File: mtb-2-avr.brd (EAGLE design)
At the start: 27 x 22 mm, 14 parts, among them IC1 MEGA8-AI, Q1 14.745 MHz

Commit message: Add LCSC parts numbers.
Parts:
- IC1: value MEGA8-AI -> MEGA328P-AU
- R3: value 1k -> 10k
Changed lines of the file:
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@@
 <layer number="20" name="Dimension" color="24" fill="1" visible="yes" active="yes"/>
 <layer number="21" name="tPlace" color="7" fill="1" visible="yes" active="yes"/>
-<layer number="22" name="bPlace" color="7" fill="1" visible="no" active="yes"/>
+<layer number="22" name="bPlace" color="7" fill="1" visible="yes" active="yes"/>
 <layer number="23" name="tOrigins" color="15" fill="1" visible="yes" active="yes"/>
-<layer number="24" name="bOrigins" color="15" fill="1" visible="no" active="yes"/>
+<layer number="24" name="bOrigins" color="15" fill="1" visible="yes" active="yes"/>
 <layer number="25" name="tNames" color="7" fill="1" visible="no" active="yes"/>
 <layer number="26" name="bNames" color="7" fill="1" visible="no" active="yes"/>
@@
 <layer number="37" name="tTest" color="7" fill="1" visible="no" active="yes"/>
 <layer number="38" name="bTest" color="7" fill="1" visible="no" active="yes"/>
-<layer number="39" name="tKeepout" color="4" fill="11" visible="yes" active="yes"/>
-<layer number="40" name="bKeepout" color="1" fill="11" visible="yes" active="yes"/>
+<layer number="39" name="tKeepout" color="4" fill="11" visible="no" active="yes"/>
+<layer number="40" name="bKeepout" color="1" fill="11" visible="no" active="yes"/>
 <layer number="41" name="tRestrict" color="4" fill="10" visible="no" active="yes"/>
 <layer number="42" name="bRestrict" color="1" fill="10" visible="no" active="yes"/>
@@
 <layer number="44" name="Drills" color="7" fill="1" visible="no" active="yes"/>
 <layer number="45" name="Holes" color="7" fill="1" visible="no" active="yes"/>
-<layer number="46" name="Milling" color="3" fill="1" visible="no" active="yes"/>
+<layer number="46" name="Milling" color="3" fill="1" visible="yes" active="yes"/>
 <layer number="47" name="Measures" color="7" fill="1" visible="no" active="yes"/>
 <layer number="48" name="Document" color="7" fill="1" visible="no" active="yes"/>
-<layer number="49" name="Reference" color="7" fill="1" visible="no" active="yes"/>
+<layer number="49" name="Reference" color="7" fill="1" visible="yes" active="yes"/>
 <layer number="50" name="dxf" color="7" fill="1" visible="no" active="no"/>
 <layer number="51" name="tDocu" color="7" fill="1" visible="yes" active="yes"/>
-<layer number="52" name="bDocu" color="7" fill="1" visible="no" active="yes"/>
+<layer number="52" name="bDocu" color="7" fill="1" visible="yes" active="yes"/>
 <layer number="53" name="tGND_GNDA" color="7" fill="9" visible="no" active="no"/>
 <layer number="54" name="bGND_GNDA" color="1" fill="9" visible="no" active="no"/>
@@
 <text x="5.715" y="3.81" size="1.016" layer="22" rot="MR0" align="bottom-center">MTB-UNI
 v2 upgrade</text>
-<text x="24.765" y="16.51" size="1.016" layer="26" rot="MR90" align="bottom-center">v1.0 JH 2021</text>
+<text x="24.765" y="16.51" size="1.016" layer="22" rot="MR90" align="bottom-center">v1.0 JH 2021</text>
 <text x="4.1275" y="16.1925" size="1.27" layer="21" rot="SR180">⏚</text>
 </plain>
@@
 </autorouter>
 <elements>
-<element name="IC1" library="atmel" library_urn="urn:adsk.eagle:library:105" package="TQFP32-08" package3d_urn="urn:adsk.eagle:package:4313/2" value="MEGA8-AI" x="17.145" y="15.875" smashed="yes" rot="R180">
+<element name="IC1" library="atmel" library_urn="urn:adsk.eagle:library:105" package="TQFP32-08" package3d_urn="urn:adsk.eagle:package:4313/2" value="MEGA328P-AU" x="17.145" y="15.875" smashed="yes" rot="R180">
+<attribute name="LCSC_PART" value="C14877" x="17.145" y="15.875" size="1.778" layer="27" rot="R180" display="off"/>
 <attribute name="MF" value="" x="-0.635" y="20.955" size="1.778" layer="27" rot="R180" display="off"/>
 <attribute name="MPN" value="ATMEGA8-16AU" x="-0.635" y="20.955" size="1.778" layer="27" rot="R180" display="off"/>
@@
 <element name="TORIG" library="mtb-2" package="DIL20" value="" x="13.335" y="5.08" smashed="yes"/>
 <element name="C1" library="rcl" package="C0603" value="100n" x="24.765" y="16.1925" smashed="yes" rot="R270">
+<attribute name="LCSC_PART" value="C14663" x="24.765" y="16.1925" size="1.778" layer="27" rot="R270" display="off"/>
 <attribute name="NAME" x="25.7175" y="16.8275" size="0.8128" layer="25" rot="R270"/>
 <attribute name="VALUE" x="22.225" y="17.4625" size="1.27" layer="27" rot="R270"/>
 </element>
 <element name="R1" library="rcl" package="R0603" value="10k" x="24.765" y="19.685" smashed="yes" rot="R270">
+<attribute name="LCSC_PART" value="C25804" x="24.765" y="19.685" size="1.778" layer="27" rot="R270" display="off"/>
 <attribute name="NAME" x="25.7175" y="20.32" size="0.8128" layer="25" rot="R270"/>
 <attribute name="VALUE" x="22.225" y="20.955" size="1.27" layer="27" rot="R270"/>
 </element>
 <element name="LED1" library="led" library_urn="urn:adsk.eagle:library:259" package="CHIPLED_0603" package3d_urn="urn:adsk.eagle:package:15822/2" value="GREEN" x="5.08" y="13.0175" smashed="yes" rot="R90">
+<attribute name="LCSC_PART" value="C72043" x="5.08" y="13.0175" size="1.778" layer="27" rot="R90" display="off"/>
 <attribute name="NAME" x="6.35" y="12.065" size="0.8128" layer="25" rot="R180"/>
 <attribute name="POPULARITY" value="28" x="5.08" y="13.0175" size="1.778" layer="27" rot="R90" display="off"/>
@@
 </element>
 <element name="LED2" library="led" library_urn="urn:adsk.eagle:library:259" package="CHIPLED_0603" package3d_urn="urn:adsk.eagle:package:15822/2" value="BLUE" x="5.08" y="14.9225" smashed="yes" rot="R90">
+<attribute name="LCSC_PART" value="C72041" x="5.08" y="14.9225" size="1.778" layer="27" rot="R90" display="off"/>
 <attribute name="NAME" x="6.35" y="16.51" size="0.8128" layer="25" rot="R180"/>
 <attribute name="POPULARITY" value="28" x="5.08" y="14.9225" size="1.778" layer="27" rot="R90" display="off"/>
@@
 </element>
 <element name="C2" library="rcl" package="C0603" value="22p" x="23.495" y="5.08" smashed="yes" rot="R180">
+<attribute name="LCSC_PART" value="C1653" x="23.495" y="5.08" size="1.778" layer="27" rot="R180" display="off"/>
 <attribute name="NAME" x="25.4" y="6.985" size="0.8128" layer="25" rot="R180"/>
 <attribute name="VALUE" x="24.765" y="7.62" size="1.27" layer="27" rot="R180"/>
 </element>
 <element name="C3" library="rcl" package="C0603" value="22p" x="3.175" y="6.0325" smashed="yes">
+<attribute name="LCSC_PART" value="C1653" x="3.175" y="6.0325" size="1.778" layer="27" display="off"/>
 <attribute name="NAME" x="0.635" y="6.6675" size="0.8128" layer="25"/>
 <attribute name="VALUE" x="1.905" y="3.4925" size="1.27" layer="27"/>
 </element>
 <element name="C4" library="rcl" package="C0603" value="100n" x="11.1125" y="15.875" smashed="yes" rot="R270">
+<attribute name="LCSC_PART" value="C14663" x="11.1125" y="15.875" size="1.778" layer="27" rot="R270" display="off"/>
 <attribute name="NAME" x="10.4775" y="14.2875" size="0.8128" layer="25" rot="R270"/>
 <attribute name="VALUE" x="8.5725" y="17.145" size="1.27" layer="27" rot="R270"/>
@@
 <element name="ISP1" library="adafruit" library_urn="urn:adsk.eagle:library:420" package="AVRISP" package3d_urn="urn:adsk.eagle:package:6240744/1" value="AVRISP-6" x="6.6675" y="19.05" smashed="yes" rot="R270"/>
 <element name="R2" library="rcl" package="R0603" value="10k" x="3.175" y="4.1275" smashed="yes">
+<attribute name="LCSC_PART" value="C25804" x="3.175" y="4.1275" size="1.778" layer="27" display="off"/>
 <attribute name="NAME" x="2.54" y="2.54" size="0.8128" layer="25"/>
 <attribute name="VALUE" x="2.54" y="1.5875" size="1.27" layer="27"/>
 </element>
-<element name="R3" library="rcl" package="R0603" value="1k" x="8.255" y="13.0175" smashed="yes">
+<element name="R3" library="rcl" package="R0603" value="10k" x="8.255" y="13.0175" smashed="yes">
+<attribute name="LCSC_PART" value="C25804" x="8.255" y="13.0175" size="1.778" layer="27" display="off"/>
 <attribute name="NAME" x="7.62" y="11.43" size="0.8128" layer="25"/>
 <attribute name="VALUE" x="7.62" y="10.4775" size="1.27" layer="27"/>
 </element>
 <element name="R4" library="rcl" package="R0603" value="1k" x="8.255" y="14.9225" smashed="yes">
+<attribute name="LCSC_PART" value="C21190" x="8.255" y="14.9225" size="1.778" layer="27" display="off"/>
 <attribute name="NAME" x="7.62" y="15.5575" size="0.8128" layer="25"/>
 <attribute name="VALUE" x="7.62" y="12.3825" size="1.27" layer="27"/>

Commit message: Minor fixes.
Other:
- board text added: "MISO"
- board text added: "MOSI"
- board text added: "VCC"
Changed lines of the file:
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@@
 <setting verticaltext="up"/>
 </settings>
-<grid distance="0.635" unitdist="mm" unit="mm" style="dots" multiple="2" display="no" altdistance="0.3175" altunitdist="mm" altunit="mm"/>
+<grid distance="0.635" unitdist="mm" unit="mil" style="dots" multiple="2" display="no" altdistance="12.5" altunitdist="mil" altunit="mil"/>
 <layers>
 <layer number="1" name="Top" color="3" fill="1" visible="yes" active="yes"/>
@@
 <text x="24.765" y="16.51" size="1.016" layer="22" rot="MR90" align="bottom-center">v1.0 JH 2021</text>
 <text x="4.1275" y="16.1925" size="1.27" layer="21" rot="SR180">⏚</text>
+<text x="4.1275" y="16.1925" size="1.27" layer="22" rot="MR270" align="center-left">⏚</text>
+<text x="6.6675" y="16.1925" size="1.27" layer="22" rot="MR270" align="center-left">MOSI</text>
+<text x="8.89" y="16.1925" size="1.27" layer="22" rot="MR270" align="center-left">VCC</text>
+<text x="10.795" y="20.6375" size="1.27" layer="22" rot="MR180" align="center-left">MISO</text>
 </plain>
 <attributes>
@@
 <element name="LED1" library="led" library_urn="urn:adsk.eagle:library:259" package="CHIPLED_0603" package3d_urn="urn:adsk.eagle:package:15822/2" value="GREEN" x="5.08" y="13.0175" smashed="yes" rot="R90">
 <attribute name="LCSC_PART" value="C72043" x="5.08" y="13.0175" size="1.778" layer="27" rot="R90" display="off"/>
-<attribute name="NAME" x="6.35" y="12.065" size="0.8128" layer="25" rot="R180"/>
+<attribute name="NAME" x="6.985" y="12.065" size="0.8128" layer="25" rot="R180"/>
 <attribute name="POPULARITY" value="28" x="5.08" y="13.0175" size="1.778" layer="27" rot="R90" display="off"/>
 <attribute name="VALUE" x="6.35" y="15.5575" size="1.27" layer="27" rot="R180"/>
@@
 <element name="LED2" library="led" library_urn="urn:adsk.eagle:library:259" package="CHIPLED_0603" package3d_urn="urn:adsk.eagle:package:15822/2" value="BLUE" x="5.08" y="14.9225" smashed="yes" rot="R90">
 <attribute name="LCSC_PART" value="C72041" x="5.08" y="14.9225" size="1.778" layer="27" rot="R90" display="off"/>
-<attribute name="NAME" x="6.35" y="16.51" size="0.8128" layer="25" rot="R180"/>
+<attribute name="NAME" x="6.985" y="16.51" size="0.8128" layer="25" rot="R180"/>
 <attribute name="POPULARITY" value="28" x="5.08" y="14.9225" size="1.778" layer="27" rot="R90" display="off"/>
 <attribute name="VALUE" x="6.35" y="17.4625" size="1.27" layer="27" rot="R180"/>
 </element>
 <element name="Q1" library="crystal" library_urn="urn:adsk.eagle:library:204" package="HC49UP" package3d_urn="urn:adsk.eagle:package:12078/1" value="14.745 MHz" x="13.335" y="5.08" smashed="yes">
+<attribute name="LCSC_PART" value="C19646" x="13.335" y="5.08" size="1.778" layer="27" display="off"/>
 <attribute name="MF" value="" x="13.335" y="5.08" size="1.778" layer="27" display="off"/>
 <attribute name="MPN" value="" x="13.335" y="5.08" size="1.778" layer="27" display="off"/>
-<attribute name="NAME" x="7.62" y="7.874" size="1.27" layer="25" ratio="10"/>
+<attribute name="NAME" x="5.3975" y="2.4765" size="1.27" layer="25" ratio="10"/>
 <attribute name="OC_FARNELL" value="unknown" x="13.335" y="5.08" size="1.778" layer="27" display="off"/>
 <attribute name="OC_NEWARK" value="unknown" x="13.335" y="5.08" size="1.778" layer="27" display="off"/>
@@
 <element name="R3" library="rcl" package="R0603" value="10k" x="8.255" y="13.0175" smashed="yes">
 <attribute name="LCSC_PART" value="C25804" x="8.255" y="13.0175" size="1.778" layer="27" display="off"/>
-<attribute name="NAME" x="7.62" y="11.43" size="0.8128" layer="25"/>
+<attribute name="NAME" x="8.255" y="11.43" size="0.8128" layer="25"/>
 <attribute name="VALUE" x="7.62" y="10.4775" size="1.27" layer="27"/>
 </element>
 <element name="R4" library="rcl" package="R0603" value="1k" x="8.255" y="14.9225" smashed="yes">
 <attribute name="LCSC_PART" value="C21190" x="8.255" y="14.9225" size="1.778" layer="27" display="off"/>
-<attribute name="NAME" x="7.62" y="15.5575" size="0.8128" layer="25"/>
+<attribute name="NAME" x="8.255" y="15.5575" size="0.8128" layer="25"/>
 <attribute name="VALUE" x="7.62" y="12.3825" size="1.27" layer="27"/>
 </element>
@@
 <via x="18.415" y="14.9225" extent="1-16" drill="0.35"/>
 <via x="19.05" y="14.9225" extent="1-16" drill="0.35"/>
-<via x="15.875" y="15.875" extent="1-16" drill="0.35"/>
-<via x="15.875" y="16.51" extent="1-16" drill="0.35"/>
-<via x="0.9525" y="6.0325" extent="1-16" drill="0.35"/>
-<via x="0.9525" y="5.3975" extent="1-16" drill="0.35"/>
-<via x="0.9525" y="4.7625" extent="1-16" drill="0.35"/>
-<via x="0.9525" y="4.1275" extent="1-16" drill="0.35"/>
+<via x="16.03375" y="15.875" extent="1-16" drill="0.35"/>
+<via x="16.03375" y="16.51" extent="1-16" drill="0.35"/>
+<via x="1.11125" y="6.0325" extent="1-16" drill="0.35"/>
+<via x="1.11125" y="5.3975" extent="1-16" drill="0.35"/>
+<via x="1.11125" y="4.7625" extent="1-16" drill="0.35"/>
+<via x="1.11125" y="4.1275" extent="1-16" drill="0.35"/>
 <via x="5.08" y="6.985" extent="1-16" drill="0.35"/>
 <via x="5.715" y="6.985" extent="1-16" drill="0.35"/>

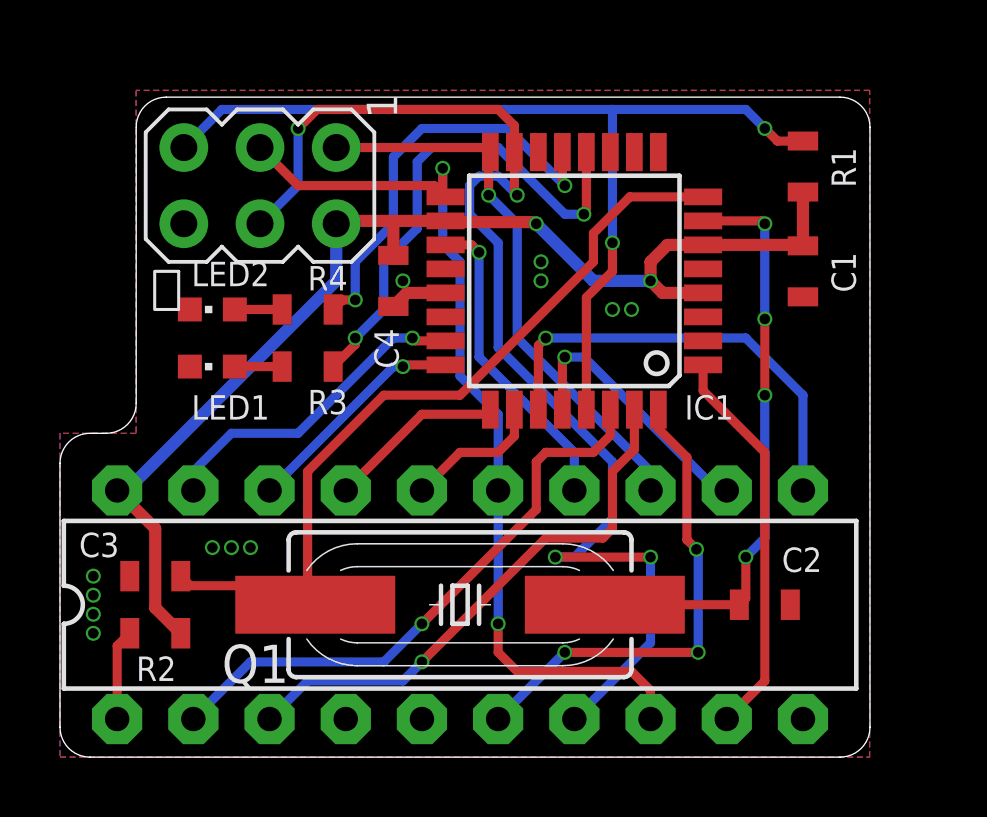
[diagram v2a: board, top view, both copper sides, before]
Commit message: Add button, rewire, remove prog. connector.
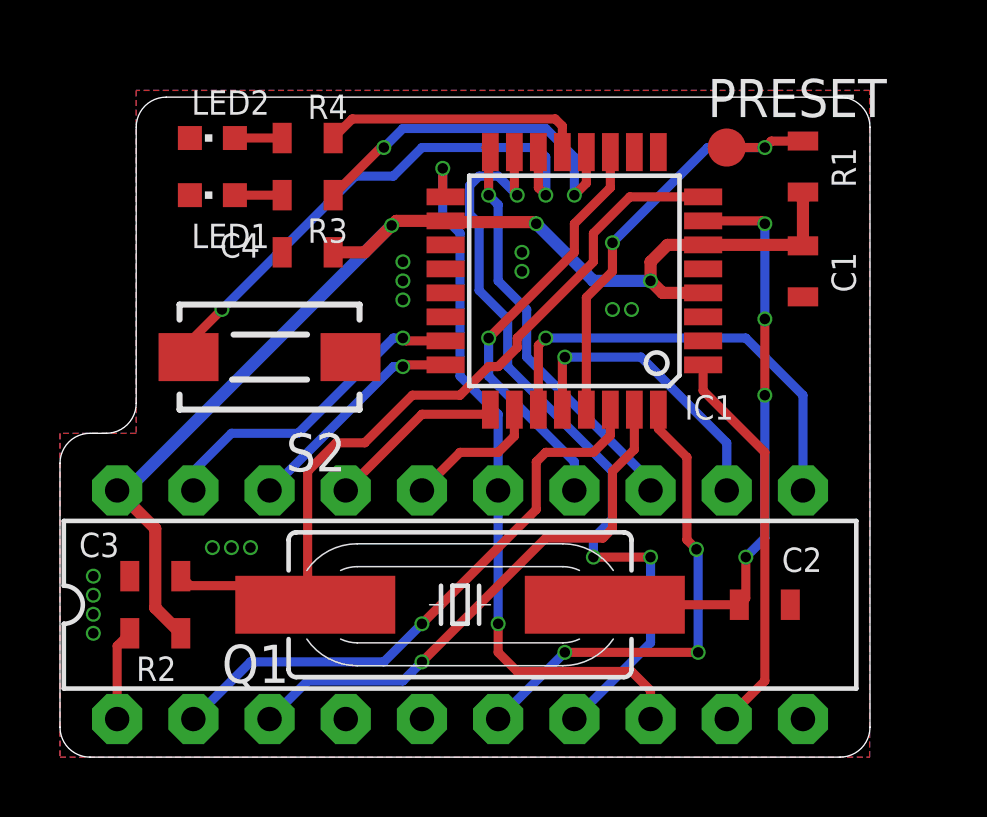
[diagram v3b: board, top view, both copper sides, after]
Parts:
- removed ISP1: AVRISP-6, adafruit:AVRISP
- added PRESET: PTR1B1,27, testpad:B1,27
- added S2: DTSM-3, switch-tact:DTSM-3
- moved LED1 5.72 mm to (5.08, 18.7)
- moved R3 5.72 mm to (8.26, 18.7)
- moved LED2 5.71 mm to (5.08, 20.6)
- moved R4 5.71 mm to (8.26, 20.6)
- moved C4 3.01 mm to (8.26, 16.8), turned to 180 degrees
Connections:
- new net N$5: IC1.14, S2.2
- net GND: now also S2.1; no longer ISP1.6
- net IN_LOAD: now also IC1.11; no longer IC1.19
- net MISO: no longer ISP1.1
- net MOSI: no longer ISP1.4
- net RESET: now also PRESET.TP; no longer ISP1.5
- net SCK: no longer ISP1.3
- net VCC: no longer ISP1.2
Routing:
- net N$5: track 0.00 -> 18.0 mm, vias 0 -> 2
- net RESET: track 32.0 -> 14.9 mm
- net MOSI: track 40.9 -> 26.4 mm, vias 4 -> 3
- net SCK: track 31.2 -> 24.5 mm
- net LED_BLUE: track 14.2 -> 8.87 mm, vias 2 -> 0
- net MISO: track 18.7 -> 13.8 mm
- net LED_GREEN: track 16.8 -> 12.2 mm
- net IN_LOAD: track 10.5 -> 14.1 mm
- net GND: track 1.93 -> 0.00 mm, vias 12 -> 14
- net SCL: track 9.03 -> 9.96 mm
- net VCC: track 39.9 -> 40.0 mm, vias 2 -> 3
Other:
- board text added: "SCK"
